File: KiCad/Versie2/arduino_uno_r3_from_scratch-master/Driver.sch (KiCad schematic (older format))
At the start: 6 parts, among them U1 L298, U3 74AHC1G04, U4 74AHC1G04

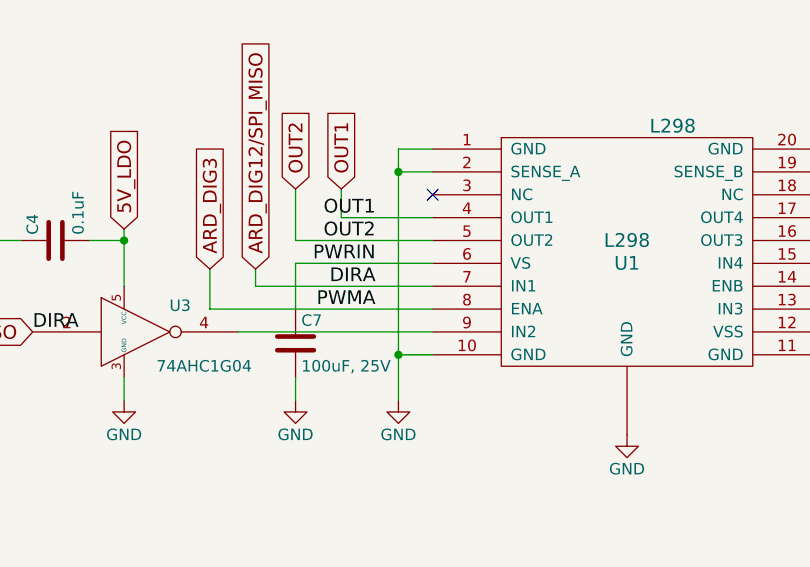
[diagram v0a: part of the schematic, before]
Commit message: 28feb
Aanpassing KiCad+deel footprints
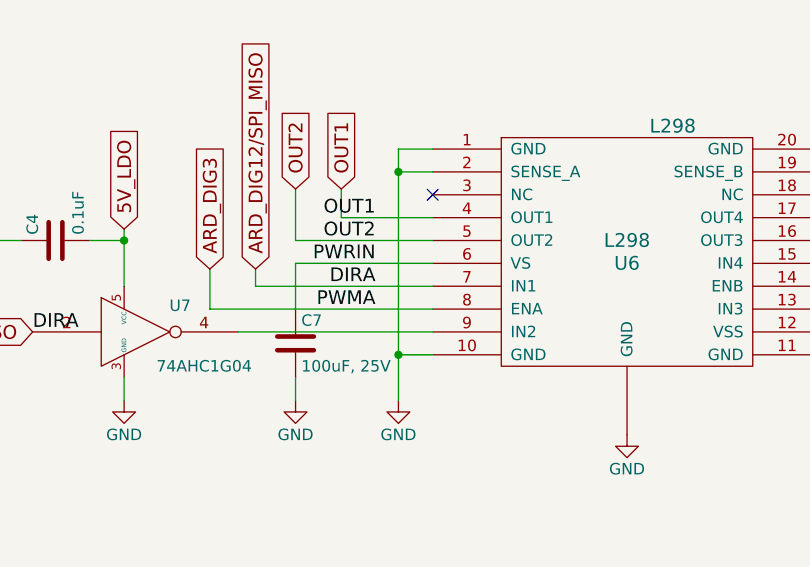
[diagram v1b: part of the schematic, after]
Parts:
- renumbered U1 to U6, U3 to U7
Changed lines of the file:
@@
 DIRB
 $Comp
-L L298 U1
+L L298 U6
 U 1 1 5A0B4B28
 P 5250 2700
-F 0 "U1" H 5250 2700 60  0000 C CNN
+F 0 "U6" H 5250 2700 60  0000 C CNN
 F 1 "L298" H 5250 2800 60  0000 C CNN
 F 2 "L298" H 5450 3300 60  0000 C CNN
@@
 	3800 3200 3800 3300
 $Comp
-L 74AHC1G04 U3
+L 74AHC1G04 U7
 U 1 1 5A0B58F7
 P 3100 3000
-F 0 "U3" H 3295 3115 50  0000 C CNN
+F 0 "U7" H 3295 3115 50  0000 C CNN
 F 1 "74AHC1G04" H 3400 2850 50  0000 C CNN
 F 2 "" H 3100 3000 50  0001 C CNN
